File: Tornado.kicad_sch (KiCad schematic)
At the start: 42 parts, among them J1 MOLEX, SW1 ID, U1 AP63205WU, U2 STM32G431KBUx, U3 LSM6DSV, U4 AP2112K-3.3, U5 TCAN1057AV, Y1 32MHz

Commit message: Changed ESD diode
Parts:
- removed D2: ~, Tornado_Footprints:TVS-2020, symbol Tornado_Symbols:D_TVS_Unidirectional
- added D2: TVS, Diode_SMD:D_SOD-323, symbol Device:D_TVS
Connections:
- net +12V: now also D2.1 (A1)
- net GND: now also D2.2 (A2)
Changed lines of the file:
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@@
   (junction (at 86.36 77.47) (diameter 0) (color 0 0 0 0)
   )
+  (junction (at 31.75 39.37) (diameter 0) (color 0 0 0 0)
+  )
   (junction (at 59.69 39.37) (diameter 0) (color 0 0 0 0)
   )
@@
   (junction (at 82.55 77.47) (diameter 0) (color 0 0 0 0)
   )
-  (junction (at 30.48 39.37) (diameter 0) (color 0 0 0 0)
-  )
   (junction (at 247.65 57.15) (diameter 0) (color 0 0 0 0)
   )
@@
     (stroke (width 0) (type default))
   )
+  (wire (pts (xy 31.75 39.37) (xy 35.56 39.37))
+    (stroke (width 0) (type default))
+  )
   (wire (pts (xy 173.99 149.86) (xy 163.83 149.86))
     (stroke (width 0) (type default))
@@
     (stroke (width 0) (type default))
   )
+  (wire (pts (xy 29.21 39.37) (xy 31.75 39.37))
+    (stroke (width 0) (type default))
+  )
   (wire (pts (xy 43.18 189.23) (xy 43.18 187.96))
     (stroke (width 0) (type default))
@@
     (stroke (width 0) (type default))
   )
+  (wire (pts (xy 31.75 40.64) (xy 31.75 39.37))
+    (stroke (width 0) (type default))
+  )
   (wire (pts (xy 214.63 132.08) (xy 213.36 132.08))
     (stroke (width 0) (type default))
@@
     (stroke (width 0) (type default))
   )
-  (wire (pts (xy 30.48 36.83) (xy 30.48 39.37))
-    (stroke (width 0) (type default))
-  )
   (wire (pts (xy 82.55 77.47) (xy 78.74 77.47))
     (stroke (width 0) (type default))
@@
     (stroke (width 0) (type default))
   )
-  (wire (pts (xy 30.48 39.37) (xy 35.56 39.37))
-    (stroke (width 0) (type default))
-  )
   (wire (pts (xy 151.13 137.16) (xy 153.67 137.16))
     (stroke (width 0) (type default))
@@
     (stroke (width 0) (type default))
   )
+  (wire (pts (xy 29.21 36.83) (xy 29.21 39.37))
+    (stroke (width 0) (type default))
+  )
   (wire (pts (xy 41.91 120.65) (xy 41.91 121.92))
     (stroke (width 0) (type default))
@@
     (stroke (width 0) (type default))
   )
+  (wire (pts (xy 31.75 49.53) (xy 31.75 48.26))
+    (stroke (width 0) (type default))
+  )
   (polyline (pts (xy 50.8 62.23) (xy 50.8 101.6))
     (stroke (width 0) (type dash))
@@
     (stroke (width 0) (type default))
   )
-  (wire (pts (xy 30.48 46.99) (xy 30.48 49.53))
-    (stroke (width 0) (type default))
-  )
   (wire (pts (xy 109.22 85.09) (xy 109.22 90.17))
     (stroke (width 0) (type default))
@@
     )
   )
-  (symbol (lib_id "power:+12V") (at 30.48 36.83 0) (unit 1)
+  (symbol (lib_id "power:+12V") (at 29.21 36.83 0) (unit 1)
     (in_bom yes) (on_board yes) (dnp no) (fields_autoplaced)
-    (property "Reference" "#PWR01" (at 30.48 40.64 0)
+    (property "Reference" "#PWR01" (at 29.21 40.64 0)
       (effects (font (size 1.27 1.27)) hide)
     )
-    (property "Value" "+12V" (at 30.48 31.75 0)
+    (property "Value" "+12V" (at 29.21 31.75 0)
       (effects (font (size 1.27 1.27)))
     )
-    (property "Footprint" "" (at 30.48 36.83 0)
+    (property "Footprint" "" (at 29.21 36.83 0)
       (effects (font (size 1.27 1.27)) hide)
     )
-    (property "Datasheet" "" (at 30.48 36.83 0)
+    (property "Datasheet" "" (at 29.21 36.83 0)
       (effects (font (size 1.27 1.27)) hide)
     )
@@
     )
   )
+  (symbol (lib_id "Device:D_TVS") (at 31.75 44.45 270) (unit 1)
+    (in_bom yes) (on_board yes) (dnp no) (fields_autoplaced)
+    (property "Reference" "D2" (at 34.29 43.18 90)
+      (effects (font (size 1.27 1.27)) (justify left))
+    )
+    (property "Value" "TVS" (at 34.29 45.72 90)
+      (effects (font (size 1.27 1.27)) (justify left))
+    )
+    (property "Footprint" "Diode_SMD:D_SOD-323" (at 31.75 44.45 0)
+      (effects (font (size 1.27 1.27)) hide)
+    )
+    (property "Datasheet" "~" (at 31.75 44.45 0)
+      (effects (font (size 1.27 1.27)) hide)
+    )
+    (pin "2")
+    (pin "1")
+    (instances
+      (project "Tornado"
+        (path "/74d9931a-8786-4de9-b7a7-1d1158c87647"
+          (reference "D2") (unit 1)
+        )
+      )
+    )
+  )
   (symbol (lib_id "power:GND") (at 257.81 86.36 0) (unit 1)
     (in_bom yes) (on_board yes) (dnp no) (fields_autoplaced)
@@
     )
   )
-  (symbol (lib_id "power:GND") (at 30.48 49.53 0) (unit 1)
+  (symbol (lib_id "power:GND") (at 31.75 49.53 0) (unit 1)
     (in_bom yes) (on_board yes) (dnp no) (fields_autoplaced)
-    (property "Reference" "#PWR02" (at 30.48 55.88 0)
+    (property "Reference" "#PWR02" (at 31.75 55.88 0)
       (effects (font (size 1.27 1.27)) hide)
     )
-    (property "Value" "GND" (at 30.48 54.61 0)
+    (property "Value" "GND" (at 31.75 54.61 0)
       (effects (font (size 1.27 1.27)))
     )
-    (property "Footprint" "" (at 30.48 49.53 0)
+    (property "Footprint" "" (at 31.75 49.53 0)
       (effects (font (size 1.27 1.27)) hide)
     )
-    (property "Datasheet" "" (at 30.48 49.53 0)
+    (property "Datasheet" "" (at 31.75 49.53 0)
       (effects (font (size 1.27 1.27)) hide)
     )
@@
         )
       )
-    )
-  )
-  (symbol (lib_id "Tornado_Symbols:D_TVS_Unidirectional") (at 30.48 43.18 270) (unit 1)
-    (in_bom yes) (on_board yes) (dnp no)
-    (property "Reference" "D2" (at 25.4 43.18 90)
-      (effects (font (size 1.27 1.27)) (justify left))
-    )
-    (property "Value" "~" (at 26.035 43.18 0)
-      (effects (font (size 1.27 1.27)))
-    )
-    (property "Footprint" "Tornado_Footprints:TVS-2020" (at 27.94 43.18 0)
-      (effects (font (size 1.27 1.27)) hide)
-    )
-    (property "Datasheet" "" (at 27.94 43.18 0)
-      (effects (font (size 1.27 1.27)) hide)
-    )
-    (pin "1")
-    (pin "2")
-    (instances
-      (project "Tornado"
-        (path "/74d9931a-8786-4de9-b7a7-1d1158c87647"
-          (reference "D2") (unit 1)
-        )
-      )

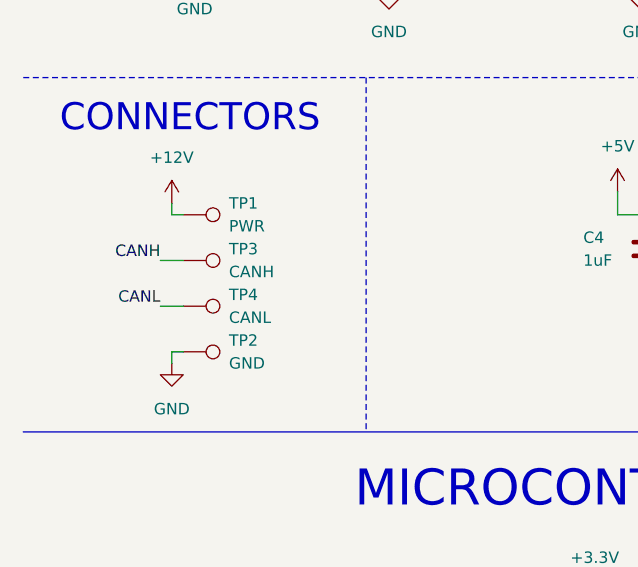
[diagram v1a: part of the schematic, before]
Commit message: Replaced pads with holes
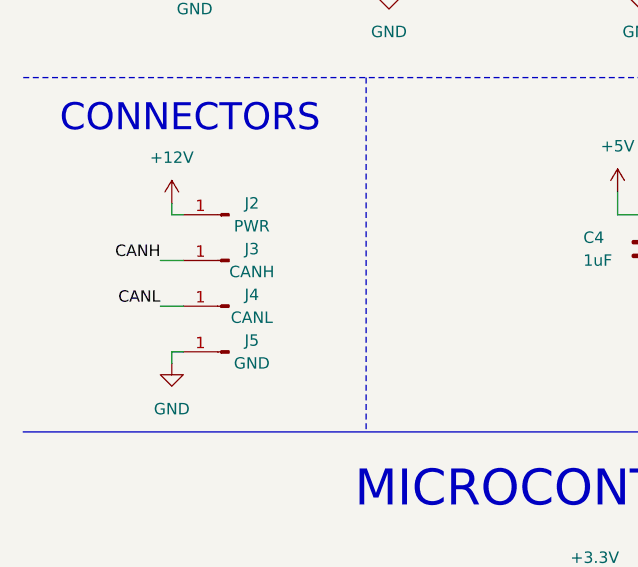
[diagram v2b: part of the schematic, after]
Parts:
- removed TP1: PWR, Tornado_Footprints:Wire_Pad, symbol Connector:TestPoint
- removed TP2: GND, Tornado_Footprints:Wire_Pad, symbol Connector:TestPoint
- removed TP3: CANH, Tornado_Footprints:Wire_Pad, symbol Connector:TestPoint
- removed TP4: CANL, Tornado_Footprints:Wire_Pad, symbol Connector:TestPoint
- added J2: PWR, Tornado_Footprints:Wire_Hole, symbol Connector:Conn_01x01_Pin
- added J3: CANH, Tornado_Footprints:Wire_Hole, symbol Connector:Conn_01x01_Pin
- added J4: CANL, Tornado_Footprints:Wire_Hole, symbol Connector:Conn_01x01_Pin
- added J5: GND, Tornado_Footprints:Wire_Hole, symbol Connector:Conn_01x01_Pin
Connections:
- net +12V: now also J2.1 (Pin_1)
- net CANH: now also J3.1 (Pin_1)
- net CANL: now also J4.1 (Pin_1)
- net GND: now also J5.1 (Pin_1)
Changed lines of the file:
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@@
     (effects (font (size 1.27 1.27)) (justify right bottom))
+  )
+  (symbol (lib_id "Connector:Conn_01x01_Pin") (at 35.56 87.63 180) (unit 1)
+    (in_bom yes) (on_board yes) (dnp no)
+    (property "Reference" "J4" (at 38.1 86.36 0)
+      (effects (font (size 1.27 1.27)))
+    )
+    (property "Value" "CANL" (at 38.1 88.9 0)
+      (effects (font (size 1.27 1.27)))
+    )
+    (property "Footprint" "Tornado_Footprints:Wire_Hole" (at 35.56 87.63 0)
+      (effects (font (size 1.27 1.27)) hide)
+    )
+    (property "Datasheet" "~" (at 35.56 87.63 0)
+      (effects (font (size 1.27 1.27)) hide)
+    )
+    (pin "1")
+    (instances
+      (project "Tornado"
+        (path "/74d9931a-8786-4de9-b7a7-1d1158c87647"
+          (reference "J4") (unit 1)
+        )
+      )
+    )
   )
   (symbol (lib_id "Device:Crystal_GND24_Small") (at 41.91 134.62 270) (unit 1)
@@
         (path "/74d9931a-8786-4de9-b7a7-1d1158c87647"
           (reference "R3") (unit 1)
+        )
+      )
+    )
+  )
+  (symbol (lib_id "Connector:Conn_01x01_Pin") (at 35.56 77.47 180) (unit 1)
+    (in_bom yes) (on_board yes) (dnp no)
+    (property "Reference" "J2" (at 38.1 76.2 0)
+      (effects (font (size 1.27 1.27)))
+    )
+    (property "Value" "PWR" (at 38.1 78.74 0)
+      (effects (font (size 1.27 1.27)))
+    )
+    (property "Footprint" "Tornado_Footprints:Wire_Hole" (at 35.56 77.47 0)
+      (effects (font (size 1.27 1.27)) hide)
+    )
+    (property "Datasheet" "~" (at 35.56 77.47 0)
+      (effects (font (size 1.27 1.27)) hide)
+    )
+    (pin "1")
+    (instances
+      (project "Tornado"
+        (path "/74d9931a-8786-4de9-b7a7-1d1158c87647"
+          (reference "J2") (unit 1)
         )
       )
@@
     )
   )
-  (symbol (lib_id "Connector:TestPoint") (at 30.48 92.71 270) (unit 1)
-    (in_bom yes) (on_board yes) (dnp no)
-    (property "Reference" "TP2" (at 35.56 91.44 90)
-      (effects (font (size 1.27 1.27)) (justify left))
-    )
-    (property "Value" "GND" (at 35.56 93.98 90)
-      (effects (font (size 1.27 1.27)) (justify left))
-    )
-    (property "Footprint" "Tornado_Footprints:Wire_Pad" (at 30.48 97.79 0)
-      (effects (font (size 1.27 1.27)) hide)
-    )
-    (property "Datasheet" "~" (at 30.48 97.79 0)
-      (effects (font (size 1.27 1.27)) hide)
-    )
-    (pin "1")
-    (instances
-      (project "Tornado"
-        (path "/74d9931a-8786-4de9-b7a7-1d1158c87647"
-          (reference "TP2") (unit 1)
-        )
-      )
-    )
-  )
   (symbol (lib_id "Device:C") (at 41.91 143.51 0) (unit 1)
     (in_bom yes) (on_board yes) (dnp no) (fields_autoplaced)
@@
         (path "/74d9931a-8786-4de9-b7a7-1d1158c87647"
           (reference "#PWR045") (unit 1)
-        )
-      )
-    )
-  )
-  (symbol (lib_id "Connector:TestPoint") (at 30.48 77.47 270) (unit 1)
-    (in_bom yes) (on_board yes) (dnp no)
-    (property "Reference" "TP1" (at 35.56 76.2 90)
-      (effects (font (size 1.27 1.27)) (justify left))
-    )
-    (property "Value" "PWR" (at 35.56 78.74 90)
-      (effects (font (size 1.27 1.27)) (justify left))
-    )
-    (property "Footprint" "Tornado_Footprints:Wire_Pad" (at 30.48 82.55 0)
-      (effects (font (size 1.27 1.27)) hide)
-    )
-    (property "Datasheet" "~" (at 30.48 82.55 0)
-      (effects (font (size 1.27 1.27)) hide)
-    )
-    (pin "1")
-    (instances
-      (project "Tornado"
-        (path "/74d9931a-8786-4de9-b7a7-1d1158c87647"
-          (reference "TP1") (unit 1)
         )
       )
@@
         (path "/74d9931a-8786-4de9-b7a7-1d1158c87647"
           (reference "D3") (unit 1)
+        )
+      )
+    )
+  )
+  (symbol (lib_id "Connector:Conn_01x01_Pin") (at 35.56 82.55 180) (unit 1)
+    (in_bom yes) (on_board yes) (dnp no)
+    (property "Reference" "J3" (at 38.1 81.28 0)
+      (effects (font (size 1.27 1.27)))
+    )
+    (property "Value" "CANH" (at 38.1 83.82 0)
+      (effects (font (size 1.27 1.27)))
+    )
+    (property "Footprint" "Tornado_Footprints:Wire_Hole" (at 35.56 82.55 0)
+      (effects (font (size 1.27 1.27)) hide)
+    )
+    (property "Datasheet" "~" (at 35.56 82.55 0)
+      (effects (font (size 1.27 1.27)) hide)
+    )
+    (pin "1")
+    (instances
+      (project "Tornado"
+        (path "/74d9931a-8786-4de9-b7a7-1d1158c87647"
+          (reference "J3") (unit 1)
         )
       )
@@
         (path "/74d9931a-8786-4de9-b7a7-1d1158c87647"
           (reference "#PWR017") (unit 1)
-        )
-      )
-    )
-  )
-  (symbol (lib_id "Connector:TestPoint") (at 30.48 82.55 270) (unit 1)
-    (in_bom yes) (on_board yes) (dnp no)
-    (property "Reference" "TP3" (at 35.56 81.28 90)
-      (effects (font (size 1.27 1.27)) (justify left))
-    )
-    (property "Value" "CANH" (at 35.56 83.82 90)
-      (effects (font (size 1.27 1.27)) (justify left))
-    )
-    (property "Footprint" "Tornado_Footprints:Wire_Pad" (at 30.48 87.63 0)
-      (effects (font (size 1.27 1.27)) hide)
-    )
-    (property "Datasheet" "~" (at 30.48 87.63 0)
-      (effects (font (size 1.27 1.27)) hide)
-    )
-    (pin "1")
-    (instances
-      (project "Tornado"
-        (path "/74d9931a-8786-4de9-b7a7-1d1158c87647"
-          (reference "TP3") (unit 1)
         )
       )
@@
     )
   )
-  (symbol (lib_id "Connector:TestPoint") (at 30.48 87.63 270) (unit 1)
-    (in_bom yes) (on_board yes) (dnp no)
-    (property "Reference" "TP4" (at 35.56 86.36 90)
-      (effects (font (size 1.27 1.27)) (justify left))
-    )
-    (property "Value" "CANL" (at 35.56 88.9 90)
-      (effects (font (size 1.27 1.27)) (justify left))
-    )
-    (property "Footprint" "Tornado_Footprints:Wire_Pad" (at 30.48 92.71 0)
-      (effects (font (size 1.27 1.27)) hide)
-    )
-    (property "Datasheet" "~" (at 30.48 92.71 0)
-      (effects (font (size 1.27 1.27)) hide)
-    )
-    (pin "1")
-    (instances
-      (project "Tornado"
-        (path "/74d9931a-8786-4de9-b7a7-1d1158c87647"
-          (reference "TP4") (unit 1)
-        )
-      )
-    )
-  )
   (symbol (lib_id "Switch:SW_Push") (at 120.65 130.81 0) (unit 1)
     (in_bom yes) (on_board yes) (dnp no) (fields_autoplaced)
@@
         )
       )
+    )
+  )
+  (symbol (lib_id "Connector:Conn_01x01_Pin") (at 35.56 92.71 180) (unit 1)
+    (in_bom yes) (on_board yes) (dnp no)
+    (property "Reference" "J5" (at 38.1 91.44 0)
+      (effects (font (size 1.27 1.27)))
+    )
+    (property "Value" "GND" (at 38.1 93.98 0)
+      (effects (font (size 1.27 1.27)))
+    )
+    (property "Footprint" "Tornado_Footprints:Wire_Hole" (at 35.56 92.71 0)
+      (effects (font (size 1.27 1.27)) hide)
+    )
+    (property "Datasheet" "~" (at 35.56 92.71 0)
+      (effects (font (size 1.27 1.27)) hide)
+    )
+    (pin "1")
+    (instances
+      (project "Tornado"
+        (path "/74d9931a-8786-4de9-b7a7-1d1158c87647"
+          (reference "J5") (unit 1)
+        )
+      )

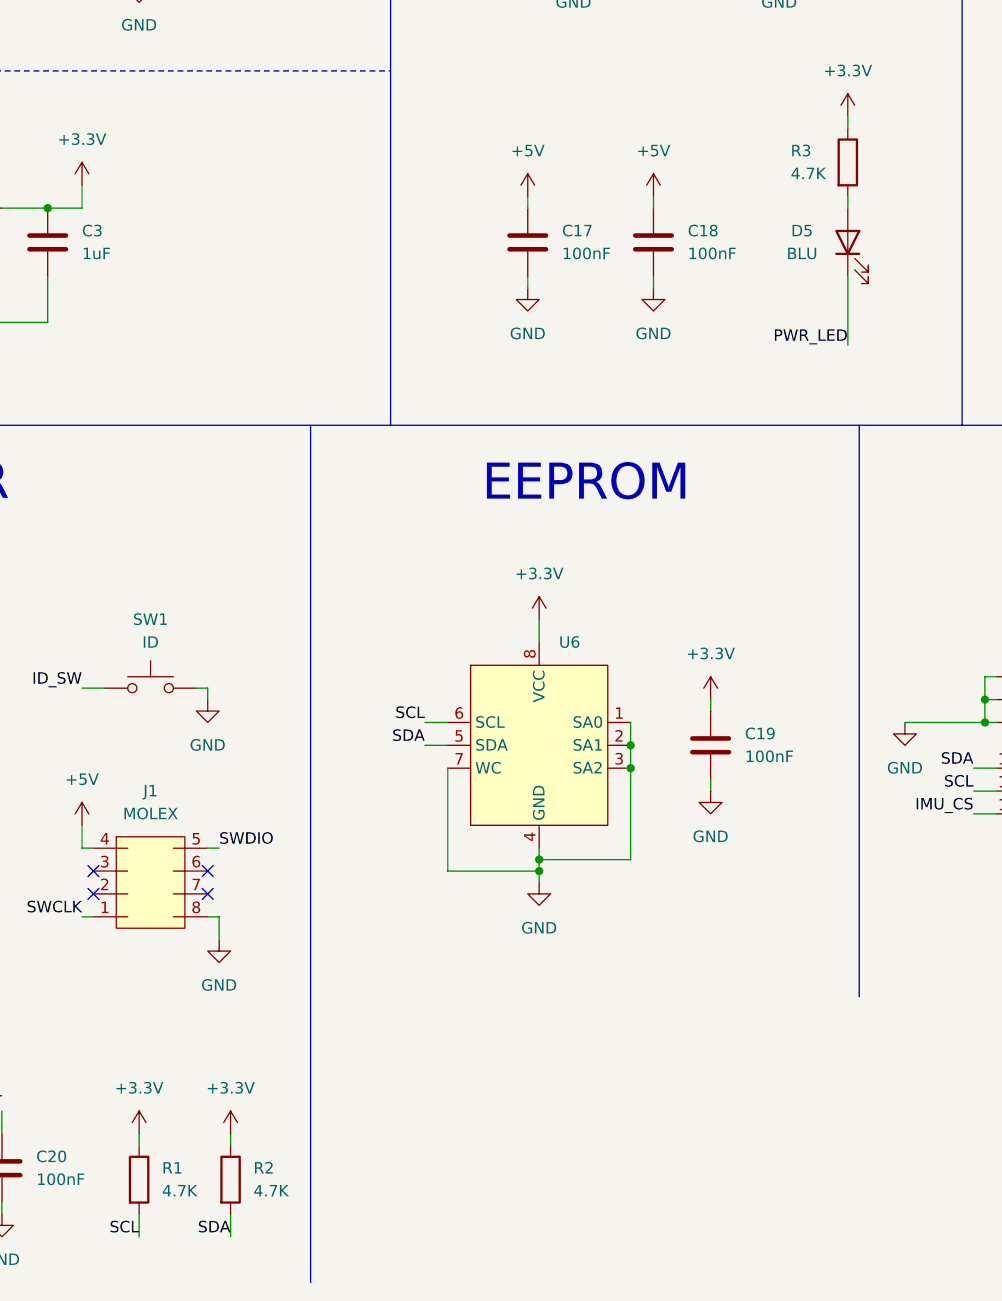
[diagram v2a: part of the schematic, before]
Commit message: Added Silkscreen
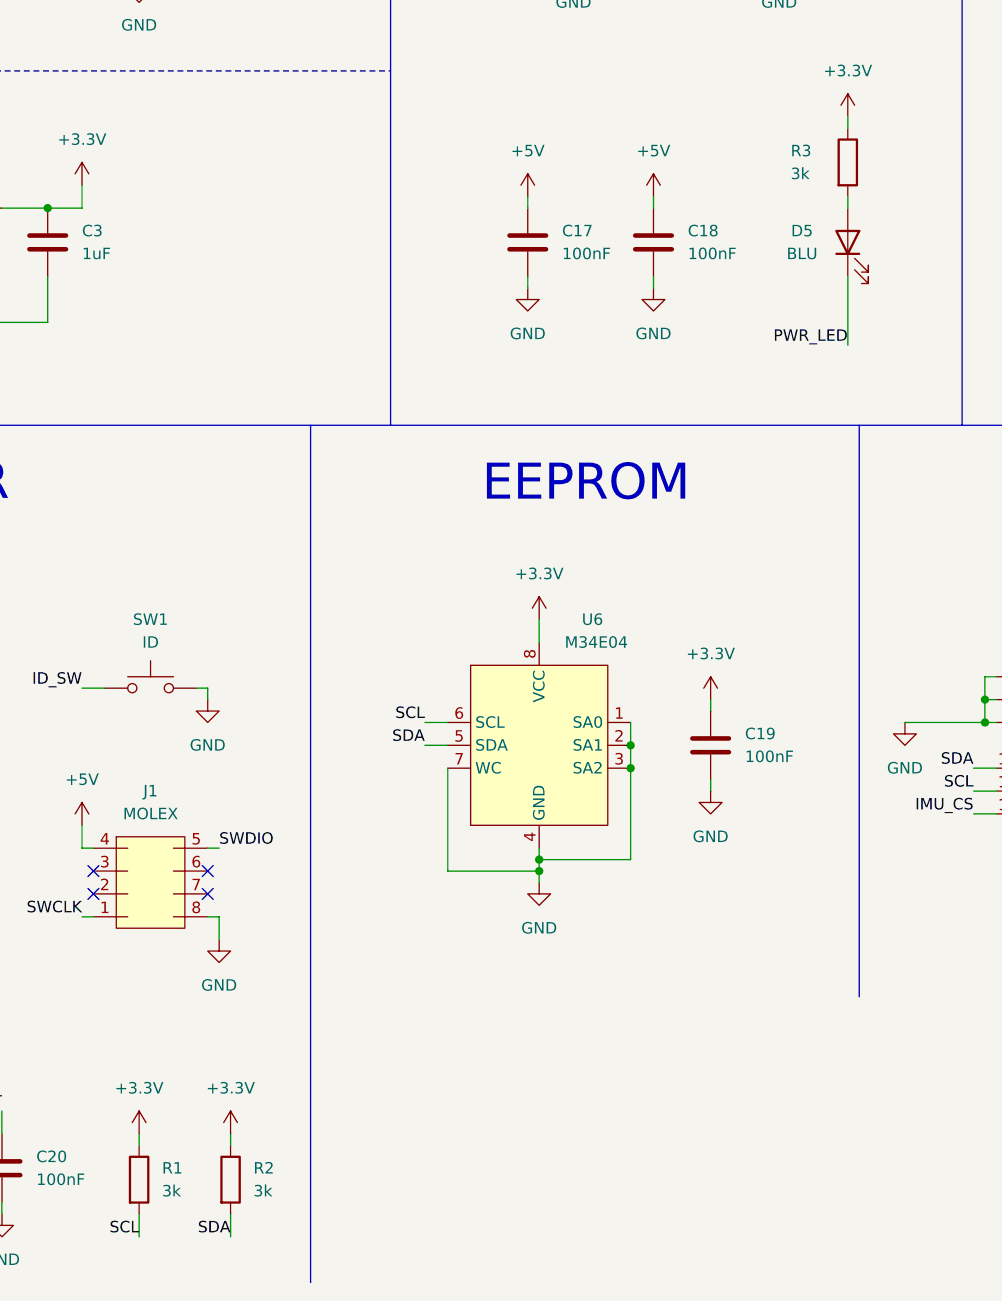
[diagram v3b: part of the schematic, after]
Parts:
- R1, R2, R3: value 4.7K -> 3k
- U6: value ~ -> M34E04
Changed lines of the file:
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@@
   (title_block
     (title "Tornado")
-    (rev "1")
+    (rev "2")
   )
   (junction (at 109.22 77.47) (diameter 0) (color 0 0 0 0)
@@
       (effects (font (size 1.27 1.27)) (justify left))
     )
-    (property "Value" "4.7K" (at 191.77 73.66 0)
+    (property "Value" "3k" (at 191.77 73.66 0)
       (effects (font (size 1.27 1.27)) (justify left))
     )
@@
       (effects (font (size 1.27 1.27)) (justify left))
     )
-    (property "Value" "4.7K" (at 132.08 186.69 0)
+    (property "Value" "3k" (at 132.08 186.69 0)
       (effects (font (size 1.27 1.27)) (justify left))
     )
@@
       (effects (font (size 1.27 1.27)) (justify left))
     )
-    (property "Value" "4.7K" (at 121.92 186.69 0)
+    (property "Value" "3k" (at 121.92 186.69 0)
       (effects (font (size 1.27 1.27)) (justify left))
     )
@@
   )
   (symbol (lib_id "Tornado_Symbols:M34E04") (at 163.83 142.24 0) (unit 1)
-    (in_bom yes) (on_board yes) (dnp no) (fields_autoplaced)
-    (property "Reference" "U6" (at 166.0241 125.73 0)
-      (effects (font (size 1.27 1.27)) (justify left))
-    )
-    (property "Value" "~" (at 173.99 146.05 0)
-      (effects (font (size 1.27 1.27)))
-    )
+    (in_bom yes) (on_board yes) (dnp no)
+    (property "Reference" "U6" (at 168.5641 123.19 0)
+      (effects (font (size 1.27 1.27)) (justify left))
+    )
+    (property "Value" "M34E04" (at 170.18 125.73 0)
+      (effects (font (size 1.27 1.27)))
+    )
